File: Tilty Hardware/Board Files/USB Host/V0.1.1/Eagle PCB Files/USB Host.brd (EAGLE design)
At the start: 38.1 x 50.8 mm, 24 parts, among them U1 MAX3421E, U2 AP7313SOT23R, U3 LM2931

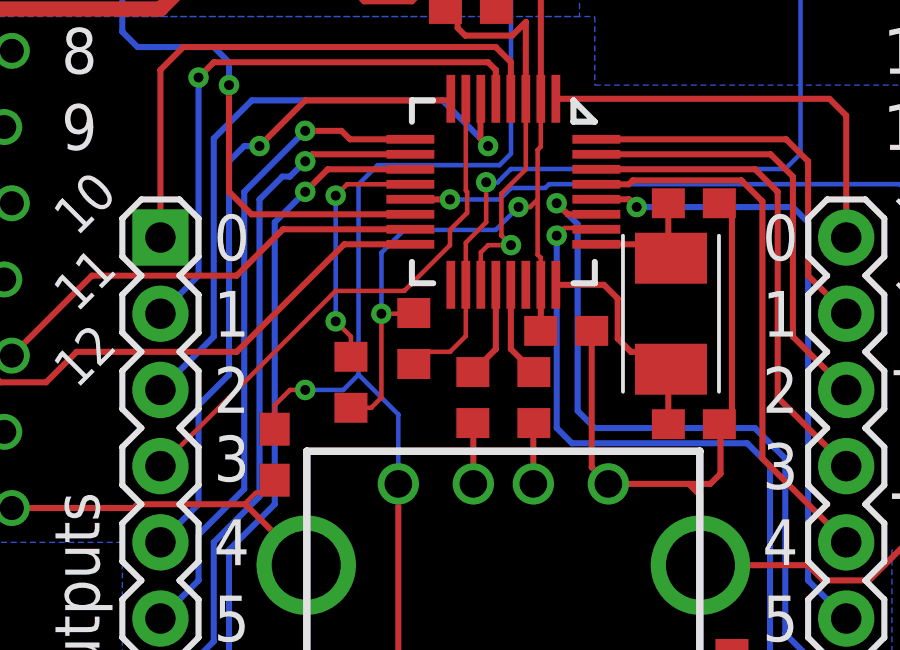
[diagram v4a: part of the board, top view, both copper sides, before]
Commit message: USB Host add-on work
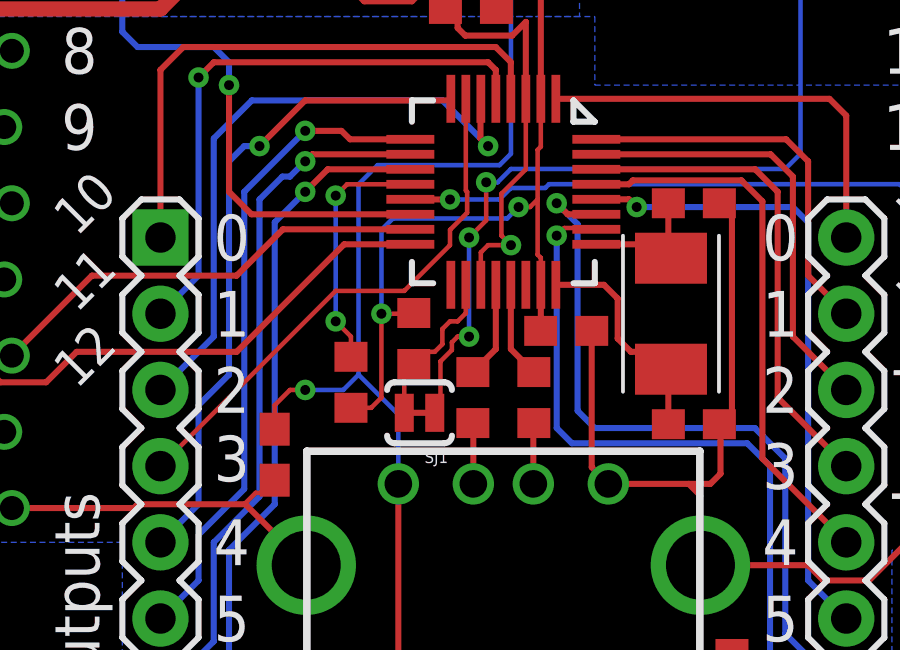
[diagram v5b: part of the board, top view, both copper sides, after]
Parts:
- added SJ1: SOLDERJUMPERTRACE, SparkFun-Passives:SJ_2S-TRACE
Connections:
- new net INT_PIN: R3.1, SJ1.2, U1.18
- net INT: now also SJ1.1; no longer R3.1, U1.18
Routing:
- net INT_PIN: track 0.00 -> 5.44 mm
- net INT: track 32.7 -> 33.8 mm, vias 1 -> 3
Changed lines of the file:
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@@
 <attribute name="VALUE" x="11.938" y="16.383" size="1.27" layer="27" rot="R270"/>
 </element>
+<element name="SJ1" library="SparkFun-Passives" package="SJ_2S-TRACE" value="SOLDERJUMPERTRACE" x="16.256" y="14.478" rot="R180"/>
 </elements>
 <signals>
@@
 <wire x1="19.558" y1="21.336" x2="19.939" y2="21.336" width="0.1524" layer="1"/>
 <wire x1="19.939" y1="21.336" x2="20.193" y2="21.59" width="0.1524" layer="1"/>
-<wire x1="14.986" y1="17.78" x2="14.986" y2="19.812" width="0.1524" layer="16"/>
-<wire x1="14.986" y1="19.812" x2="15.748" y2="20.574" width="0.1524" layer="16"/>
-<wire x1="15.748" y1="20.574" x2="18.796" y2="20.574" width="0.1524" layer="16"/>
-<wire x1="18.796" y1="20.574" x2="19.558" y2="21.336" width="0.1524" layer="16"/>
+<wire x1="14.986" y1="17.78" x2="14.986" y2="20.574" width="0.1524" layer="16"/>
 <wire x1="20.3" y1="24.944" x2="20.3" y2="28.722" width="0.2032" layer="1"/>
 <wire x1="20.3" y1="28.722" x2="19.812" y2="29.21" width="0.2032" layer="1"/>
@@
 <wire x1="14.644" y1="14.644" x2="14.986" y2="14.986" width="0.1524" layer="1"/>
 <wire x1="14.986" y1="14.986" x2="14.986" y2="17.78" width="0.1524" layer="1"/>
+<wire x1="19.558" y1="21.336" x2="19.177" y2="20.955" width="0.1524" layer="16"/>
+<wire x1="19.177" y1="20.955" x2="15.367" y2="20.955" width="0.1524" layer="16"/>
+<wire x1="15.367" y1="20.955" x2="14.986" y2="20.574" width="0.1524" layer="16"/>
 </signal>
 <signal name="+5V">
@@
 </signal>
 <signal name="INT">
-<contactref element="U1" pad="18"/>
-<contactref element="R3" pad="1"/>
 <contactref element="JP4" pad="P$6"/>
 <via x="18.4785" y="22.1615" extent="1-16" drill="0.3302"/>
-<wire x1="17.8" y1="18.744" x2="17.8" y2="20.1495" width="0.1524" layer="1"/>
-<wire x1="17.8" y1="20.1495" x2="18.4785" y2="20.828" width="0.1524" layer="1"/>
-<wire x1="18.4785" y1="20.828" x2="18.4785" y2="22.1615" width="0.1524" layer="1"/>
+<wire x1="18.4785" y1="20.8915" x2="18.4785" y2="22.1615" width="0.1524" layer="1"/>
 <wire x1="18.4785" y1="22.1615" x2="18.8595" y2="22.1615" width="0.1524" layer="16"/>
 <wire x1="18.8595" y1="22.1615" x2="19.304" y2="22.606" width="0.1524" layer="16"/>
@@
 <wire x1="28.956" y1="23.114" x2="28.956" y2="35.052" width="0.1524" layer="16"/>
 <wire x1="28.956" y1="35.052" x2="30.607" y2="36.703" width="0.1524" layer="16"/>
-<wire x1="17.8" y1="18.744" x2="17.8" y2="17.038" width="0.1524" layer="1"/>
-<wire x1="17.8" y1="17.038" x2="17.272" y2="16.51" width="0.1524" layer="1"/>
-<wire x1="17.272" y1="16.51" x2="16.471" y2="16.51" width="0.1524" layer="1"/>
-<wire x1="16.471" y1="16.51" x2="16.0655" y2="16.1045" width="0.1524" layer="1"/>
+<contactref element="SJ1" pad="1"/>
+<via x="17.907" y="20.32" extent="1-16" drill="0.3302"/>
+<wire x1="18.4785" y1="20.8915" x2="17.907" y2="20.32" width="0.1524" layer="1"/>
+<via x="17.907" y="17.018" extent="1-16" drill="0.3302"/>
+<wire x1="17.907" y1="20.32" x2="17.907" y2="17.018" width="0.1524" layer="16"/>
+<wire x1="17.907" y1="17.018" x2="17.526" y2="17.018" width="0.1524" layer="1"/>
+<wire x1="17.526" y1="17.018" x2="17.3355" y2="16.8275" width="0.1524" layer="1"/>
+<wire x1="17.3355" y1="16.8275" x2="17.3355" y2="16.5735" width="0.1524" layer="1"/>
+<wire x1="17.3355" y1="16.5735" x2="16.9545" y2="16.1925" width="0.1524" layer="1"/>
+<wire x1="16.9545" y1="16.1925" x2="16.9545" y2="14.6685" width="0.1524" layer="1"/>
+<wire x1="16.9545" y1="14.6685" x2="16.764" y2="14.478" width="0.1524" layer="1"/>
 </signal>
 <signal name="RST">
@@
 <wire x1="33.274" y1="7.962" x2="33.694" y2="8.382" width="0.2032" layer="1"/>
 </signal>
+<signal name="INT_PIN">
+<contactref element="U1" pad="18"/>
+<contactref element="R3" pad="1"/>
+<contactref element="SJ1" pad="2"/>
+<wire x1="16.471" y1="16.51" x2="16.0655" y2="16.1045" width="0.1524" layer="1"/>
+<wire x1="16.471" y1="16.51" x2="16.764" y2="16.51" width="0.1524" layer="1"/>
+<wire x1="16.764" y1="16.51" x2="17.018" y2="16.764" width="0.1524" layer="1"/>
+<wire x1="17.018" y1="16.764" x2="17.018" y2="17.272" width="0.1524" layer="1"/>
+<wire x1="17.018" y1="17.272" x2="17.272" y2="17.526" width="0.1524" layer="1"/>
+<wire x1="17.272" y1="17.526" x2="17.526" y2="17.526" width="0.1524" layer="1"/>
+<wire x1="17.526" y1="17.526" x2="17.8" y2="17.8" width="0.1524" layer="1"/>
+<wire x1="17.8" y1="18.744" x2="17.8" y2="17.8" width="0.1524" layer="1"/>
+<wire x1="15.748" y1="14.478" x2="15.748" y2="15.787" width="0.1524" layer="1"/>
+<wire x1="15.748" y1="15.787" x2="16.0655" y2="16.1045" width="0.1524" layer="1"/>
+</signal>
 </signals>

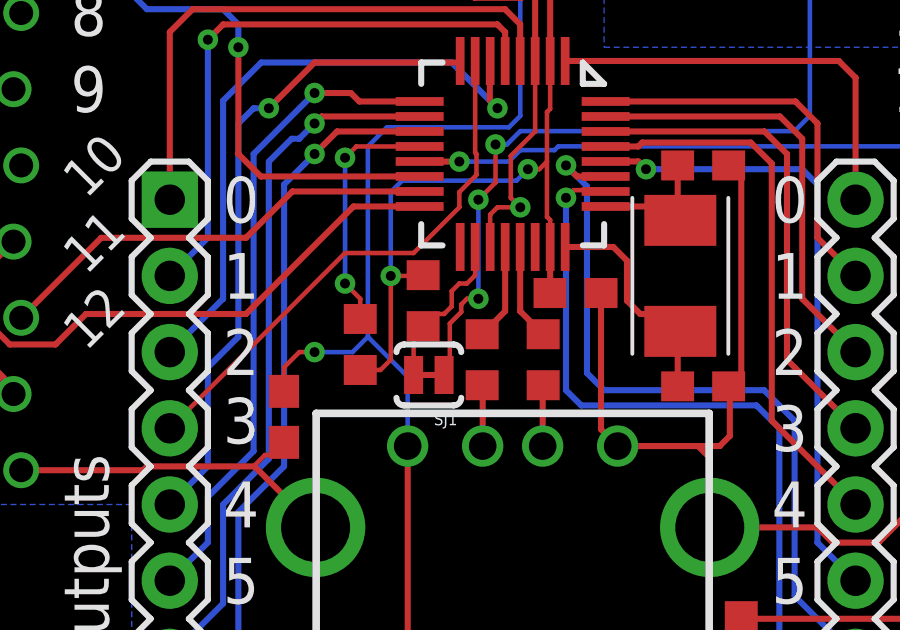
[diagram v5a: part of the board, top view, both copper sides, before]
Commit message: Altered USB host interrupt solderpad
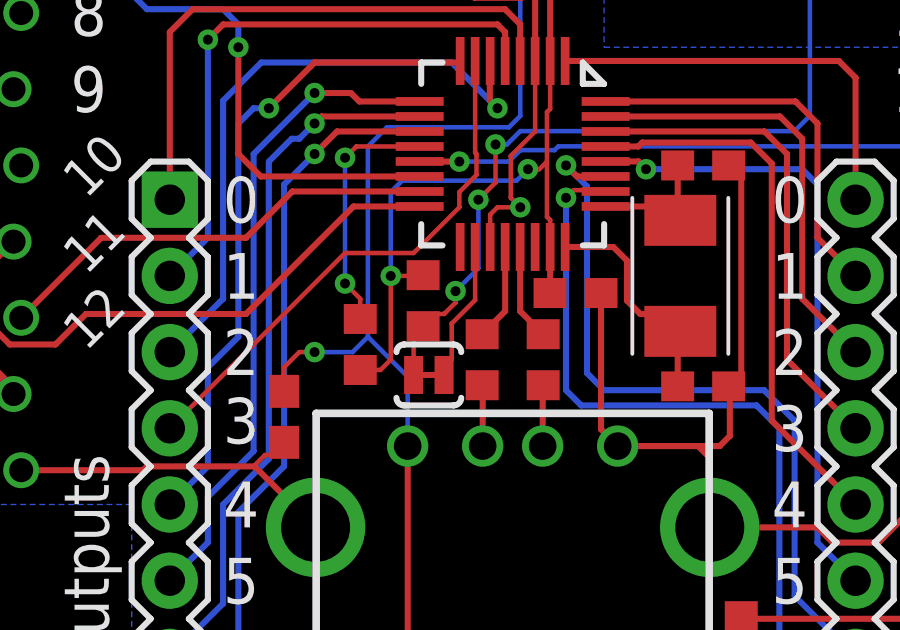
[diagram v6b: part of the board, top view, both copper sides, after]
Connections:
- removed net INT_PIN: R3.1, SJ1.2, U1.18
- new net N$10: SJ1.1, U1.18
- net INT: now also R3.1, SJ1.2; no longer SJ1.1
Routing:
- net INT_PIN: track 5.44 -> 0.00 mm
- net N$10: track 0.00 -> 4.70 mm
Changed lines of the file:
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@@
 <attribute name="VALUE" x="11.938" y="16.383" size="1.27" layer="27" rot="R270"/>
 </element>
-<element name="SJ1" library="SparkFun-Passives" package="SJ_2S-TRACE" value="SOLDERJUMPERTRACE" x="16.256" y="14.478" rot="R180"/>
+<element name="SJ1" library="SparkFun-Passives" package="SJ_2S-TRACE" value="SOLDERJUMPERTRACE" x="16.256" y="14.478" smashed="yes" rot="R180">
+<attribute name="VALUE" x="17.2085" y="16.129" size="0.4064" layer="27" rot="R180"/>
+</element>
 </elements>
 <signals>
@@
 <wire x1="28.956" y1="23.114" x2="28.956" y2="35.052" width="0.1524" layer="16"/>
 <wire x1="28.956" y1="35.052" x2="30.607" y2="36.703" width="0.1524" layer="16"/>
-<contactref element="SJ1" pad="1"/>
 <via x="17.907" y="20.32" extent="1-16" drill="0.3302"/>
 <wire x1="18.4785" y1="20.8915" x2="17.907" y2="20.32" width="0.1524" layer="1"/>
-<via x="17.907" y="17.018" extent="1-16" drill="0.3302"/>
-<wire x1="17.907" y1="20.32" x2="17.907" y2="17.018" width="0.1524" layer="16"/>
-<wire x1="17.907" y1="17.018" x2="17.526" y2="17.018" width="0.1524" layer="1"/>
-<wire x1="17.526" y1="17.018" x2="17.3355" y2="16.8275" width="0.1524" layer="1"/>
-<wire x1="17.3355" y1="16.8275" x2="17.3355" y2="16.5735" width="0.1524" layer="1"/>
-<wire x1="17.3355" y1="16.5735" x2="16.9545" y2="16.1925" width="0.1524" layer="1"/>
-<wire x1="16.9545" y1="16.1925" x2="16.9545" y2="14.6685" width="0.1524" layer="1"/>
-<wire x1="16.9545" y1="14.6685" x2="16.764" y2="14.478" width="0.1524" layer="1"/>
+<via x="17.145" y="17.272" extent="1-16" drill="0.3302"/>
+<contactref element="SJ1" pad="2"/>
+<contactref element="R3" pad="1"/>
+<wire x1="17.907" y1="20.32" x2="17.907" y2="18.034" width="0.1524" layer="16"/>
+<wire x1="17.907" y1="18.034" x2="17.145" y2="17.272" width="0.1524" layer="16"/>
+<wire x1="17.145" y1="17.272" x2="17.145" y2="16.891" width="0.1524" layer="1"/>
+<wire x1="17.145" y1="16.891" x2="16.764" y2="16.51" width="0.1524" layer="1"/>
+<wire x1="16.764" y1="16.51" x2="16.471" y2="16.51" width="0.1524" layer="1"/>
+<wire x1="16.471" y1="16.51" x2="16.0655" y2="16.1045" width="0.1524" layer="1"/>
+<wire x1="16.0655" y1="16.1045" x2="16.0655" y2="16.0655" width="0.1524" layer="1"/>
+<wire x1="16.0655" y1="16.0655" x2="15.748" y2="15.748" width="0.1524" layer="1"/>
+<wire x1="15.748" y1="15.748" x2="15.748" y2="14.478" width="0.1524" layer="1"/>
 </signal>
 <signal name="RST">
@@
 <wire x1="33.274" y1="7.962" x2="33.694" y2="8.382" width="0.2032" layer="1"/>
 </signal>
-<signal name="INT_PIN">
+<signal name="N$10">
 <contactref element="U1" pad="18"/>
-<contactref element="R3" pad="1"/>
-<contactref element="SJ1" pad="2"/>
-<wire x1="16.471" y1="16.51" x2="16.0655" y2="16.1045" width="0.1524" layer="1"/>
-<wire x1="16.471" y1="16.51" x2="16.764" y2="16.51" width="0.1524" layer="1"/>
-<wire x1="16.764" y1="16.51" x2="17.018" y2="16.764" width="0.1524" layer="1"/>
-<wire x1="17.018" y1="16.764" x2="17.018" y2="17.272" width="0.1524" layer="1"/>
-<wire x1="17.018" y1="17.272" x2="17.272" y2="17.526" width="0.1524" layer="1"/>
-<wire x1="17.272" y1="17.526" x2="17.526" y2="17.526" width="0.1524" layer="1"/>
-<wire x1="17.526" y1="17.526" x2="17.8" y2="17.8" width="0.1524" layer="1"/>
-<wire x1="17.8" y1="18.744" x2="17.8" y2="17.8" width="0.1524" layer="1"/>
-<wire x1="15.748" y1="14.478" x2="15.748" y2="15.787" width="0.1524" layer="1"/>
-<wire x1="15.748" y1="15.787" x2="16.0655" y2="16.1045" width="0.1524" layer="1"/>
+<contactref element="SJ1" pad="1"/>
+<wire x1="16.764" y1="14.478" x2="16.764" y2="14.732" width="0.1524" layer="1"/>
+<wire x1="16.764" y1="14.732" x2="17.018" y2="14.986" width="0.1524" layer="1"/>
+<wire x1="17.018" y1="14.986" x2="17.018" y2="16.1925" width="0.1524" layer="1"/>
+<wire x1="17.018" y1="16.1925" x2="17.8" y2="16.9745" width="0.1524" layer="1"/>
+<wire x1="17.8" y1="18.744" x2="17.8" y2="16.9745" width="0.1524" layer="1"/>
 </signal>
 </signals>

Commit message: LOTS of cleaning house....
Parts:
- C6: value 1uF -> ).F
- X1: value (none) -> 12MHz
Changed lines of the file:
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@@
 <attribute name="VALUE" x="20.2565" y="15.1765" size="1.27" layer="27"/>
 </element>
-<element name="X1" library="SparkFun-FreqCtrl" package="CRYSTAL-TXC-7A" value="" x="24.638" y="17.78" smashed="yes" rot="R270">
+<element name="X1" library="SparkFun-FreqCtrl" package="CRYSTAL-TXC-7A" value="12MHz" x="24.638" y="17.78" smashed="yes" rot="R270">
 <attribute name="PART#" value="7A-12.000MAAE-T" x="24.638" y="17.78" size="1.778" layer="27" rot="R270" display="off"/>
 <attribute name="VALUE" x="24.13" y="18.796003125" size="0.4064" layer="27" rot="R270"/>
@@
 </element>
 <element name="U2" library="My Parts" package="SOT23" value="AP7313SOT23R" x="18.034" y="30.48" smashed="yes"/>
-<element name="C6" library="resistor" package="C0603" value="1uF" x="17.9705" y="27.94" smashed="yes" rot="R180">
+<element name="C6" library="resistor" package="C0603" value=").F" x="17.9705" y="27.94" smashed="yes" rot="R180">
 <attribute name="VALUE" x="18.8595" y="29.972" size="1.27" layer="27" rot="R180"/>
 </element>
